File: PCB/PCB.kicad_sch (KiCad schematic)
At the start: 21 parts, among them J1 Conn_01x06_Female, J2 09252306841, U13 74HC165, U15 LT3042xMSE, U16 74HC165

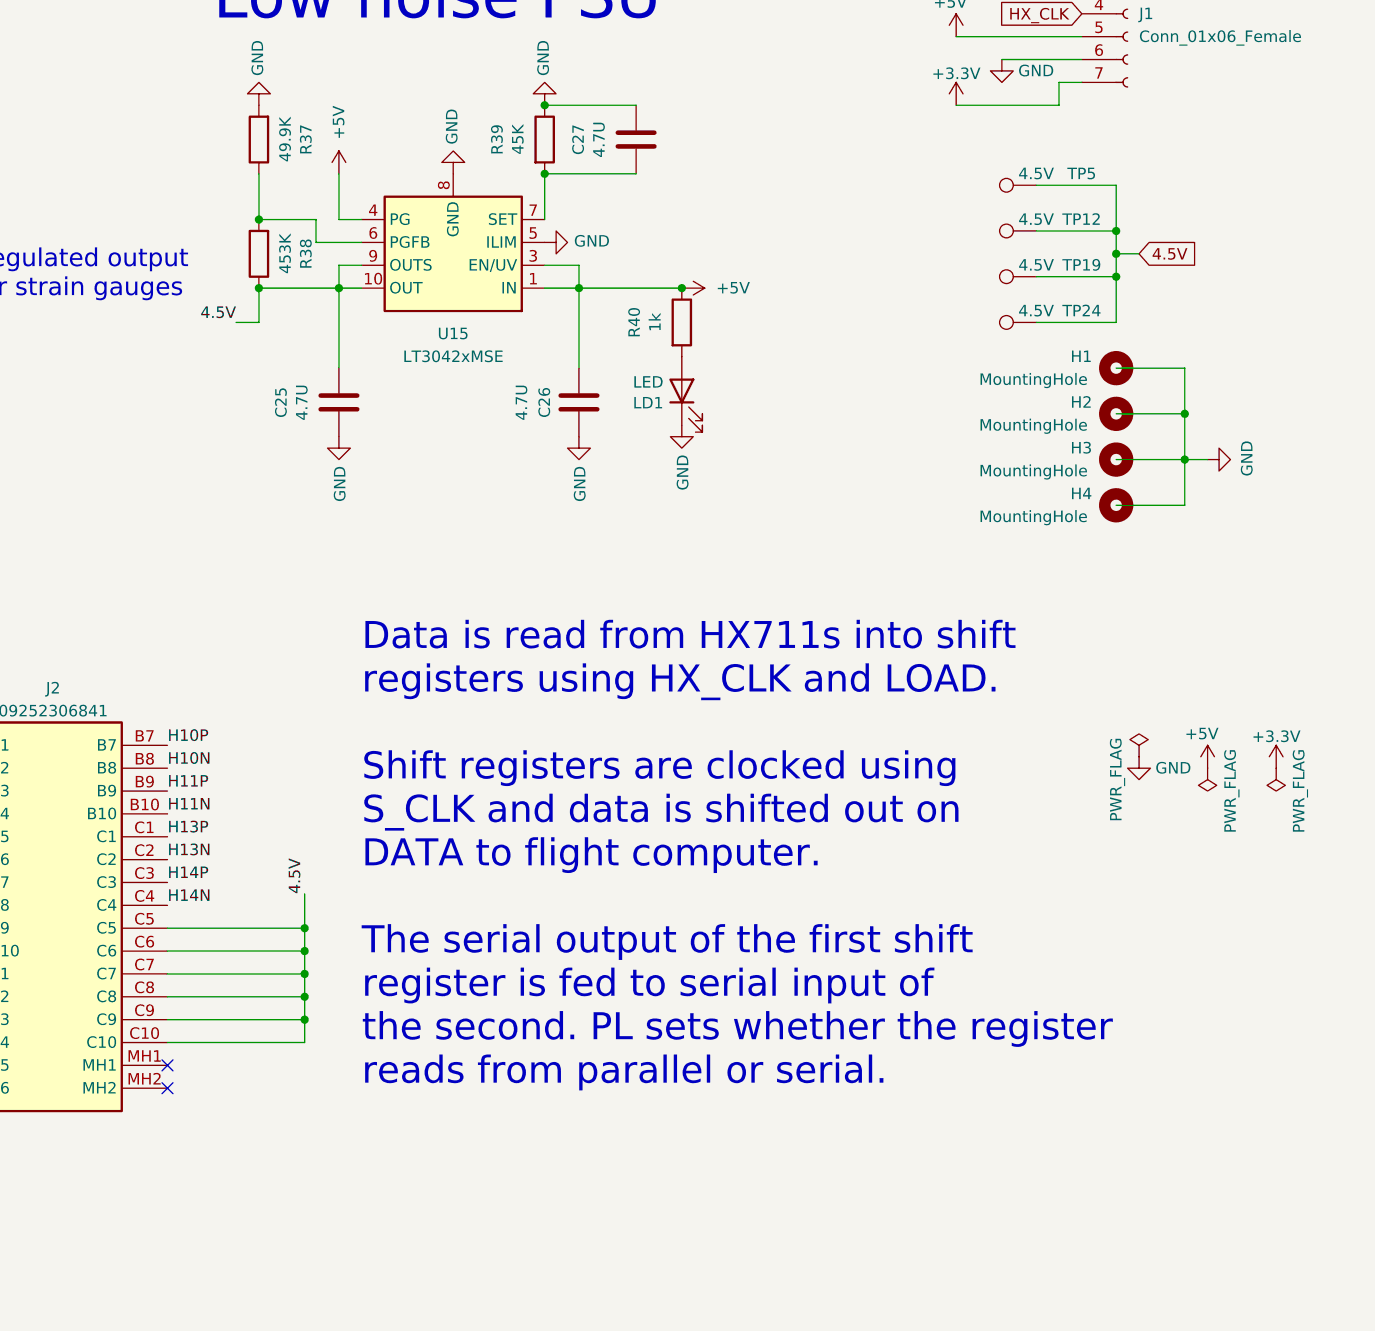
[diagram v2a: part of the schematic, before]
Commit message: Schematic update
Updated ports to ground
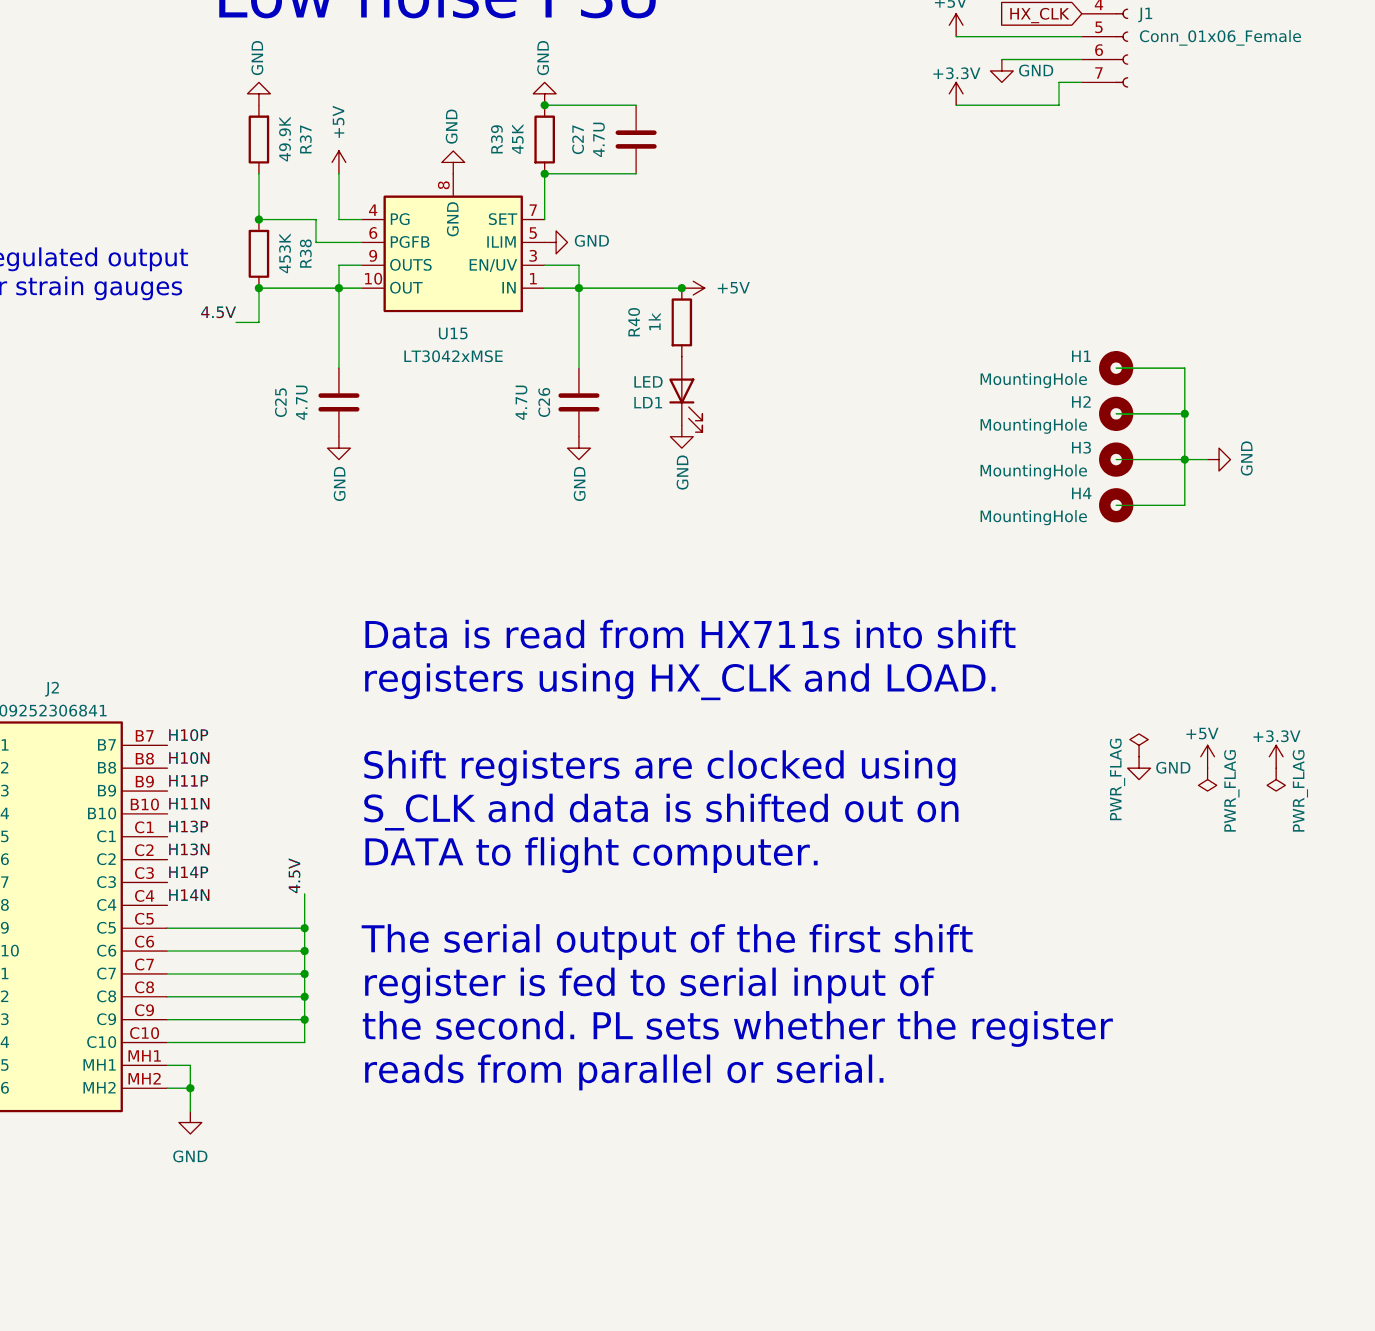
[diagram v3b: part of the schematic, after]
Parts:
- removed TP12, TP19, TP24, TP5: 4.5V, Custom-footprints:Radial-Pads-With-Relief, symbol PCB-rescue:TestPoint-Connector
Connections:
- net GND: now also J2.MH1, J2.MH2
- no-connect marks 9 -> 7
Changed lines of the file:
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@@
   (junction (at 195.58 64.77) (diameter 0) (color 0 0 0 0)
   )
-  (junction (at 255.27 60.96) (diameter 0) (color 0 0 0 0)
+  (junction (at 152.4 153.67) (diameter 0) (color 0 0 0 0)
   )
   (junction (at 20.32 177.8) (diameter 0) (color 0 0 0 0)
@@
   (junction (at 191.77 52.07) (diameter 0) (color 0 0 0 0)
   )
-  (junction (at 255.27 63.5) (diameter 0) (color 0 0 0 0)
-  )
   (junction (at 165.1 146.05) (diameter 0) (color 0 0 0 0)
   )
@@
   )
   (junction (at 165.1 135.89) (diameter 0) (color 0 0 0 0)
-  )
-  (junction (at 255.27 58.42) (diameter 0) (color 0 0 0 0)
   )
   (junction (at 191.77 44.45) (diameter 0) (color 0 0 0 0)
@@
   (no_connect (at 45.72 165.1))
   (no_connect (at 114.3 165.1))
-  (no_connect (at 149.86 151.13))
   (no_connect (at 40.64 165.1))
-  (no_connect (at 149.86 153.67))
   (no_connect (at 58.42 190.5))
   (no_connect (at 111.76 190.5))
@@
     (stroke (width 0) (type default))
   )
+  (wire (pts (xy 152.4 151.13) (xy 149.86 151.13))
+    (stroke (width 0) (type default))
+  )
   (wire (pts (xy 66.04 49.53) (xy 66.04 151.13))
     (stroke (width 0) (type default))
@@
     (stroke (width 0) (type default))
   )
-  (wire (pts (xy 255.27 58.42) (xy 255.27 60.96))
+  (wire (pts (xy 149.86 153.67) (xy 152.4 153.67))
     (stroke (width 0) (type default))
   )
@@
     (stroke (width 0) (type default))
   )
-  (wire (pts (xy 255.27 63.5) (xy 255.27 68.58))
-    (stroke (width 0) (type default))
-  )
   (wire (pts (xy 88.9 93.98) (xy 85.09 93.98))
     (stroke (width 0) (type default))
   )
-  (wire (pts (xy 246.38 53.34) (xy 255.27 53.34))
-    (stroke (width 0) (type default))
-  )
   (wire (pts (xy 166.37 57.15) (xy 166.37 59.69))
     (stroke (width 0) (type default))
@@
     (stroke (width 0) (type default))
   )
-  (wire (pts (xy 246.38 58.42) (xy 255.27 58.42))
-    (stroke (width 0) (type default))
-  )
   (wire (pts (xy 251.46 41.91) (xy 248.92 41.91))
     (stroke (width 0) (type default))
@@
     (stroke (width 0) (type default))
   )
-  (wire (pts (xy 255.27 60.96) (xy 257.81 60.96))
-    (stroke (width 0) (type default))
-  )
   (wire (pts (xy 66.04 151.13) (xy 93.98 151.13))
     (stroke (width 0) (type default))
@@
     (stroke (width 0) (type default))
   )
-  (wire (pts (xy 255.27 63.5) (xy 246.38 63.5))
-    (stroke (width 0) (type default))
-  )
   (wire (pts (xy 99.06 148.59) (xy 81.28 148.59))
     (stroke (width 0) (type default))
@@
     (stroke (width 0) (type default))
   )
-  (wire (pts (xy 255.27 53.34) (xy 255.27 58.42))
-    (stroke (width 0) (type default))
-  )
   (wire (pts (xy 96.52 149.86) (xy 96.52 165.1))
     (stroke (width 0) (type default))
@@
     (stroke (width 0) (type default))
   )
+  (wire (pts (xy 152.4 153.67) (xy 152.4 151.13))
+    (stroke (width 0) (type default))
+  )
   (wire (pts (xy 106.68 144.78) (xy 106.68 165.1))
     (stroke (width 0) (type default))
@@
     (stroke (width 0) (type default))
   )
-  (wire (pts (xy 255.27 68.58) (xy 246.38 68.58))
-    (stroke (width 0) (type default))
-  )
   (wire (pts (xy 191.77 64.77) (xy 195.58 64.77))
     (stroke (width 0) (type default))
@@
     (stroke (width 0) (type default))
   )
+  (wire (pts (xy 152.4 156.21) (xy 152.4 153.67))
+    (stroke (width 0) (type default))
+  )
   (wire (pts (xy 248.92 44.45) (xy 237.49 44.45))
-    (stroke (width 0) (type default))
-  )
-  (wire (pts (xy 255.27 60.96) (xy 255.27 63.5))
     (stroke (width 0) (type default))
   )
@@
   (label "H13N" (at 149.86 128.27 0) (fields_autoplaced)
     (effects (font (size 1.27 1.27)) (justify left bottom))
-  )
-  (global_label "4.5V" (shape input) (at 257.81 60.96 0) (fields_autoplaced)
-    (effects (font (size 1.27 1.27)) (justify left))
-    (property "Intersheetrefs" "${INTERSHEET_REFS}" (at 264.2466 60.8806 0)
-      (effects (font (size 1.27 1.27)) (justify left) hide)
-    )
   )
   (global_label "HX_CLK" (shape input) (at 251.46 34.29 180) (fields_autoplaced)
@@
     )
   )
-  (symbol (lib_id "PCB-rescue:TestPoint-Connector") (at 246.38 53.34 90) (unit 1)
-    (in_bom yes) (on_board yes) (dnp no)
-    (property "Reference" "TP5" (at 251.46 52.07 90)
-      (effects (font (size 1.27 1.27)))
-    )
-    (property "Value" "4.5V" (at 246.38 52.07 90)
-      (effects (font (size 1.27 1.27)))
-    )
-    (property "Footprint" "Custom-footprints:Radial-Pads-With-Relief" (at 246.38 48.26 0)
-      (effects (font (size 1.27 1.27)) hide)
-    )
-    (property "Datasheet" "" (at 246.38 48.26 0)
-      (effects (font (size 1.27 1.27)) hide)
-    )
-    (pin "1")
-    (instances
-      (project "PCB"
-        (path "/b6270a28-e0d9-4655-a18a-03dbf007b940"
-          (reference "TP5") (unit 1)
-        )
-      )
-    )
-  )
   (symbol (lib_id "PCB-rescue:+5V-power") (at 207.01 64.77 270) (unit 1)
     (in_bom yes) (on_board yes) (dnp no)
@@
         (path "/b6270a28-e0d9-4655-a18a-03dbf007b940"
           (reference "C27") (unit 1)
-        )
-      )
-    )
-  )
-  (symbol (lib_id "PCB-rescue:TestPoint-Connector") (at 246.38 63.5 90) (unit 1)
-    (in_bom yes) (on_board yes) (dnp no)
-    (property "Reference" "TP19" (at 251.46 62.23 90)
-      (effects (font (size 1.27 1.27)))
-    )
-    (property "Value" "4.5V" (at 246.38 62.23 90)
-      (effects (font (size 1.27 1.27)))
-    )
-    (property "Footprint" "Custom-footprints:Radial-Pads-With-Relief" (at 246.38 58.42 0)
-      (effects (font (size 1.27 1.27)) hide)
-    )
-    (property "Datasheet" "" (at 246.38 58.42 0)
-      (effects (font (size 1.27 1.27)) hide)
-    )
-    (pin "1")
-    (instances
-      (project "PCB"
-        (path "/b6270a28-e0d9-4655-a18a-03dbf007b940"
-          (reference "TP19") (unit 1)
-        )
-      )
-    )
-  )
-  (symbol (lib_id "PCB-rescue:TestPoint-Connector") (at 246.38 68.58 90) (unit 1)
-    (in_bom yes) (on_board yes) (dnp no)
-    (property "Reference" "TP24" (at 251.46 67.31 90)
-      (effects (font (size 1.27 1.27)))
-    )
-    (property "Value" "4.5V" (at 246.38 67.31 90)
-      (effects (font (size 1.27 1.27)))
-    )
-    (property "Footprint" "Custom-footprints:Radial-Pads-With-Relief" (at 246.38 63.5 0)
-      (effects (font (size 1.27 1.27)) hide)
-    )
-    (property "Datasheet" "" (at 246.38 63.5 0)
-      (effects (font (size 1.27 1.27)) hide)
-    )
-    (pin "1")
-    (instances
-      (project "PCB"
-        (path "/b6270a28-e0d9-4655-a18a-03dbf007b940"
-          (reference "TP24") (unit 1)
         )
       )
@@
         (path "/b6270a28-e0d9-4655-a18a-03dbf007b940"
           (reference "U15") (unit 1)
+        )
+      )
+    )
+  )
+  (symbol (lib_name "GND_1") (lib_id "power:GND") (at 152.4 156.21 0) (unit 1)
+    (in_bom yes) (on_board yes) (dnp no) (fields_autoplaced)
+    (property "Reference" "#PWR041" (at 152.4 162.56 0)
+      (effects (font (size 1.27 1.27)) hide)
+    )
+    (property "Value" "GND" (at 152.4 161.29 0)
+      (effects (font (size 1.27 1.27)))
+    )
+    (property "Footprint" "" (at 152.4 156.21 0)
+      (effects (font (size 1.27 1.27)) hide)
+    )
+    (property "Datasheet" "" (at 152.4 156.21 0)
+      (effects (font (size 1.27 1.27)) hide)
+    )
+    (pin "1")
+    (instances
+      (project "PCB"
+        (path "/b6270a28-e0d9-4655-a18a-03dbf007b940"
+          (reference "#PWR041") (unit 1)
         )
       )
@@
         )
       )
-    )
-  )
-  (symbol (lib_id "PCB-rescue:TestPoint-Connector") (at 246.38 58.42 90) (unit 1)
-    (in_bom yes) (on_board yes) (dnp no)
-    (property "Reference" "TP12" (at 251.46 57.15 90)
-      (effects (font (size 1.27 1.27)))
-    )
-    (property "Value" "4.5V" (at 246.38 57.15 90)
-      (effects (font (size 1.27 1.27)))
-    )
-    (property "Footprint" "Custom-footprints:Radial-Pads-With-Relief" (at 246.38 53.34 0)
-      (effects (font (size 1.27 1.27)) hide)
-    )
-    (property "Datasheet" "" (at 246.38 53.34 0)
-      (effects (font (size 1.27 1.27)) hide)
-    )
-    (pin "1")
-    (instances
-      (project "PCB"
-        (path "/b6270a28-e0d9-4655-a18a-03dbf007b940"
-          (reference "TP12") (unit 1)
-        )
-      )

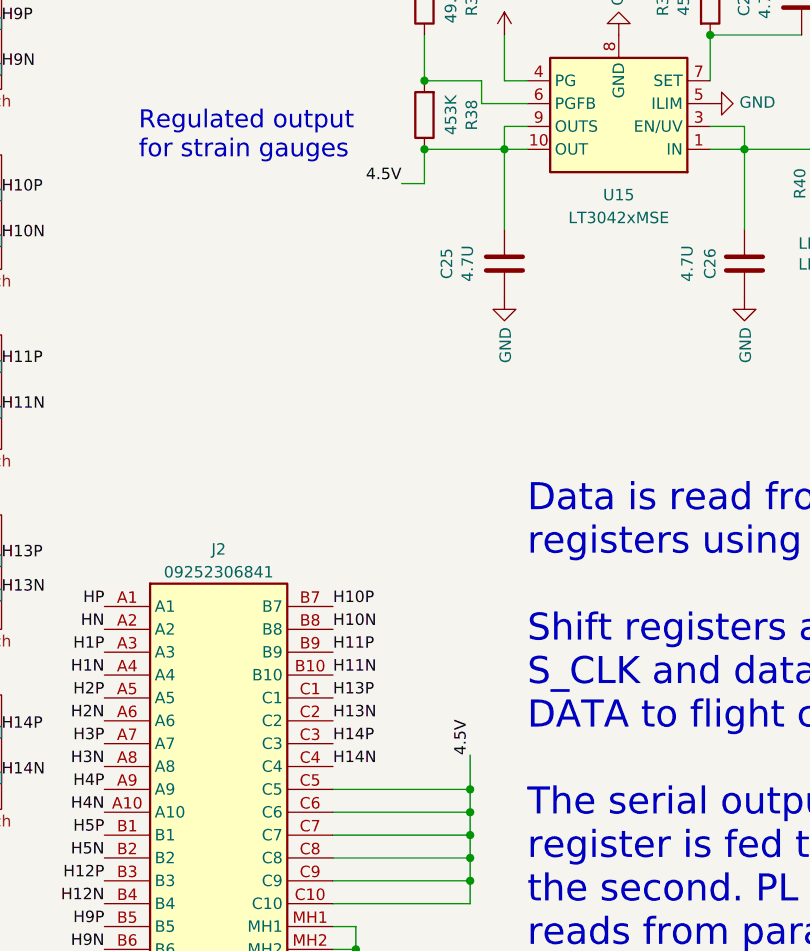
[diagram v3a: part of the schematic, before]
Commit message: Updates to layout
Started using radial, sides are going everywhere.
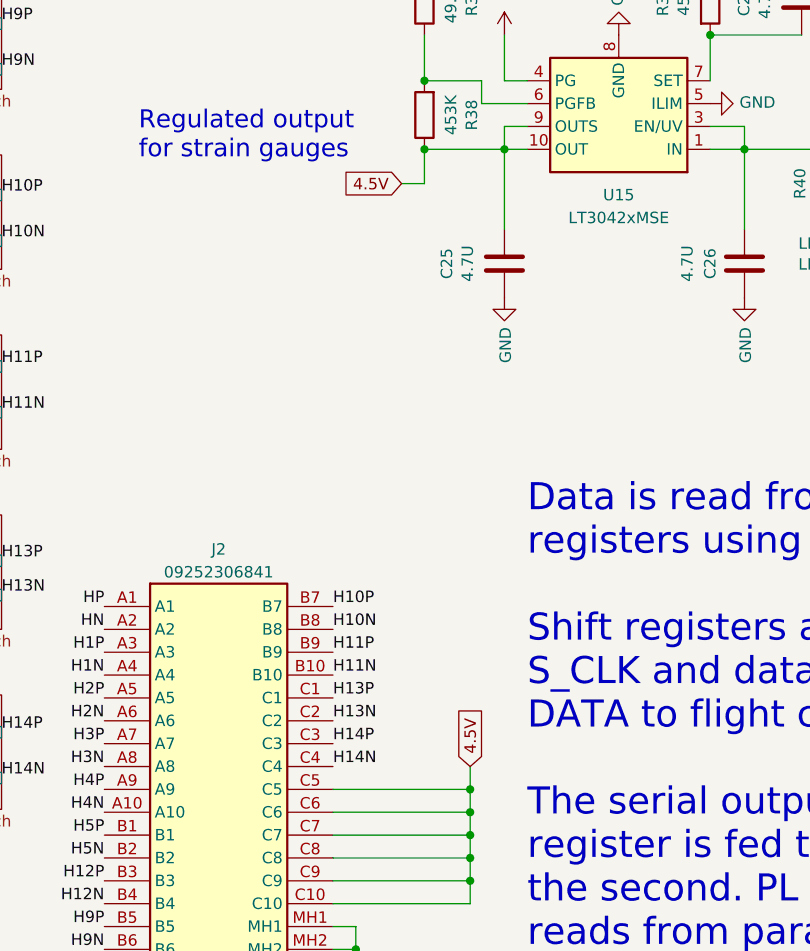
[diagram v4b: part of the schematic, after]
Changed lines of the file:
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@@
   (no_connect (at 48.26 165.1))
   (no_connect (at 43.18 165.1))
-  (wire (pts (xy 165.1 132.08) (xy 165.1 135.89))
+  (wire (pts (xy 165.1 133.35) (xy 165.1 135.89))
     (stroke (width 0) (type default))
   )
@@
     (effects (font (size 1.27 1.27)) (justify right bottom))
   )
-  (label "4.5V" (at 165.1 132.08 90) (fields_autoplaced)
-    (effects (font (size 1.27 1.27)) (justify left bottom))
-  )
   (label "H4N" (at 34.29 115.57 180) (fields_autoplaced)
     (effects (font (size 1.27 1.27)) (justify right bottom))
@@
     (effects (font (size 1.27 1.27)) (justify right bottom))
   )
-  (label "4.5V" (at 157.48 68.58 180) (fields_autoplaced)
-    (effects (font (size 1.27 1.27)) (justify right bottom))
-  )
   (label "HP" (at 34.29 30.48 180) (fields_autoplaced)
     (effects (font (size 1.27 1.27)) (justify right bottom))
@@
     (effects (font (size 1.27 1.27)) (justify left bottom))
   )
+  (global_label "4.5V" (shape input) (at 165.1 133.35 90) (fields_autoplaced)
+    (effects (font (size 1.27 1.27)) (justify left))
+    (property "Intersheetrefs" "${INTERSHEET_REFS}" (at 165.1 126.3318 90)
+      (effects (font (size 1.27 1.27)) (justify left) hide)
+    )
+  )
+  (global_label "4.5V" (shape input) (at 157.48 68.58 180) (fields_autoplaced)
+    (effects (font (size 1.27 1.27)) (justify right))
+    (property "Intersheetrefs" "${INTERSHEET_REFS}" (at 150.4618 68.58 0)
+      (effects (font (size 1.27 1.27)) (justify right) hide)
+    )
+  )
   (global_label "HX_CLK" (shape input) (at 251.46 34.29 180) (fields_autoplaced)
